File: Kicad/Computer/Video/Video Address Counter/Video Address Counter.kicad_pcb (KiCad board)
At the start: 2 copper layers, 26.7 x 90.2 mm, 22 parts, among them IC1 AP7365-33WG-7, IC10 74LVC161PW,112, IC2 74LVC573APW,118, IC3 74LVC161PW,112, IC4 74LVC161PW,112, IC5 74LVC573APW,118, IC6 74LVC161PW,112, IC7 74LVC161PW,112, IC8 74LVC573APW,118, IC9 74LVC161PW,112, J1 Conn_02x32_Counter_Clockwise

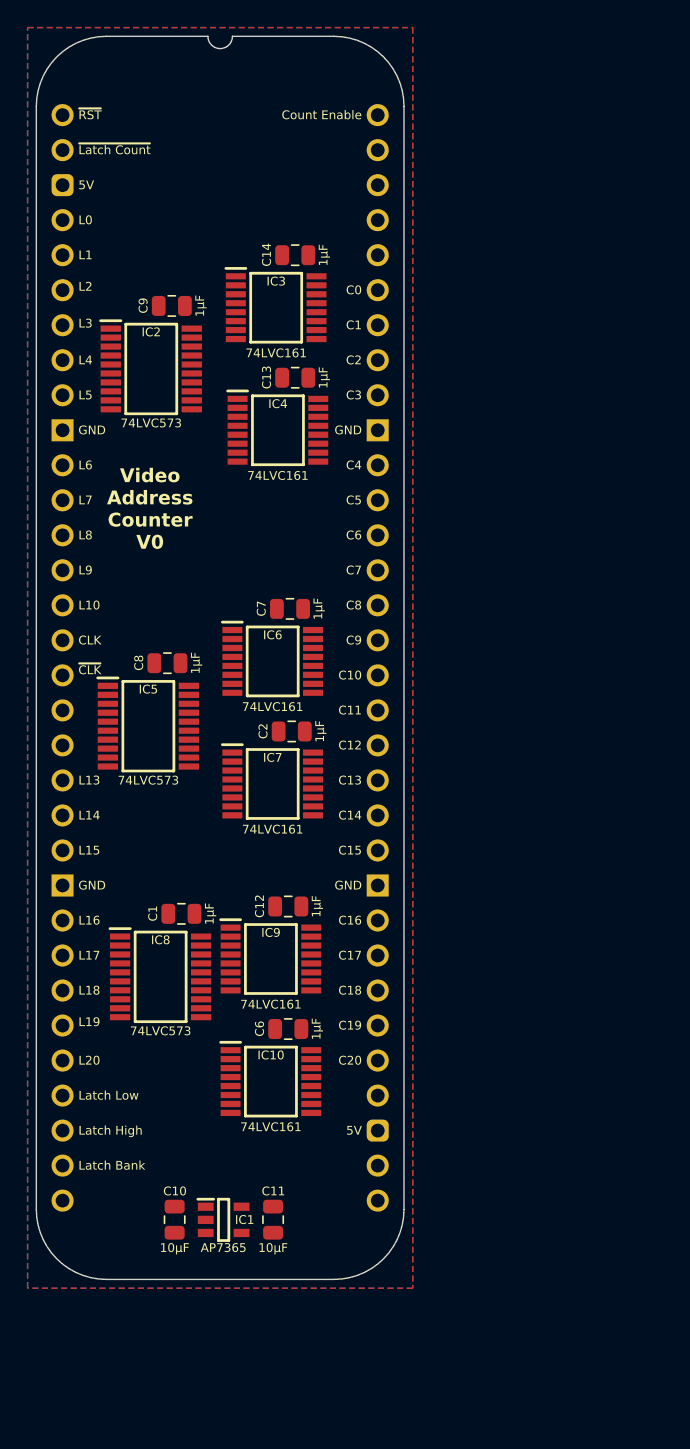
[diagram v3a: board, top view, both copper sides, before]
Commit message: Added Video Signals and Video Memory.
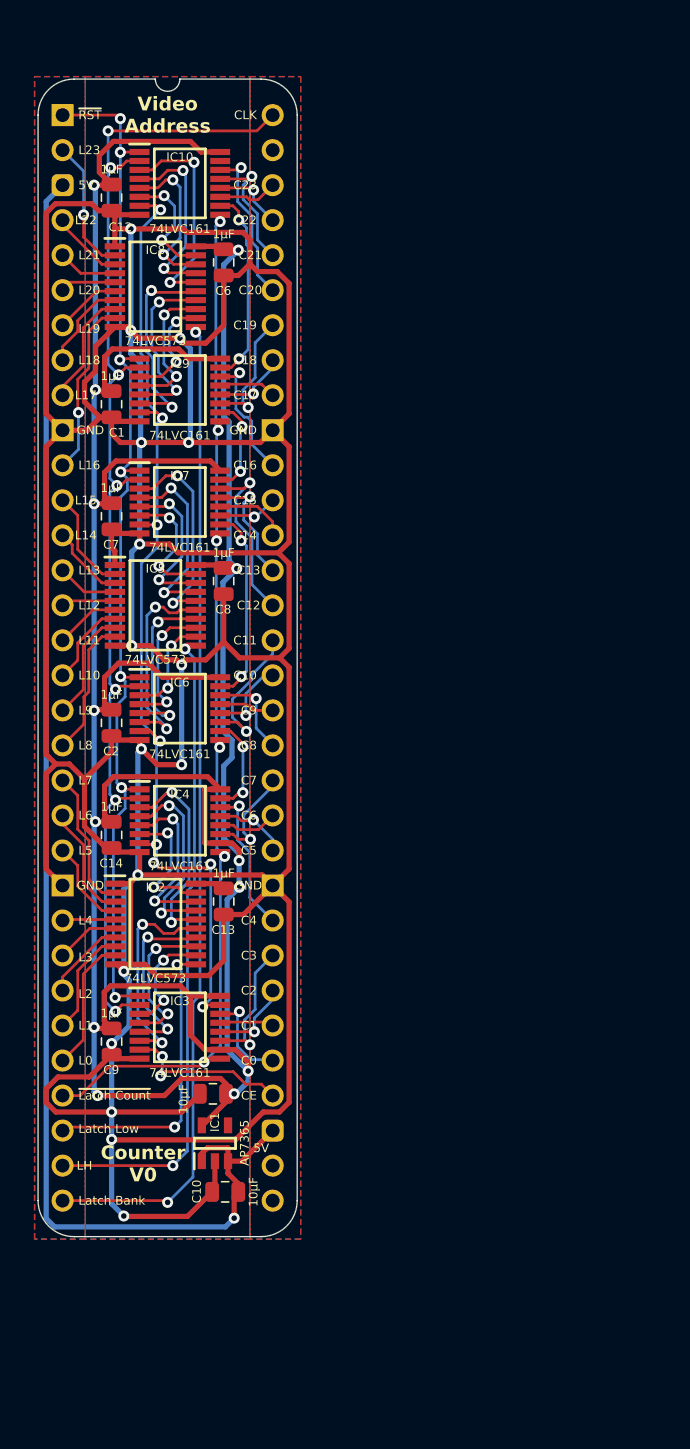
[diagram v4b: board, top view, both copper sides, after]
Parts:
- J1: footprint SamacSys_Parts:DIP-64_Board_W22.86mm -> SamacSys_Parts:DIP-64_Board_W15.24mm
- moved IC10 65.5 mm to (83.3, 53.2)
- moved C6 55.8 mm to (86.5, 58.9), turned to 180 degrees
- moved C9 53.5 mm to (78.4, 115.4), turned to 180 degrees
- moved C12 53.0 mm to (78.4, 54.2), turned to 180 degrees
- moved IC3 52.7 mm to (83.3, 114.4)
- moved IC8 50.1 mm to (81.5, 60.7)
- moved C14 44.1 mm to (78.4, 100.5), turned to 180 degrees
- moved IC9 41.8 mm to (83.3, 68.2)
- moved IC2 40.3 mm to (81.5, 106.9)
- moved C13 38.3 mm to (86.5, 105.3), turned to 180 degrees
- moved C1 37.3 mm to (78.4, 69.2), turned to 180 degrees
- moved IC4 29.2 mm to (83.3, 99.4)
- moved IC7 21.5 mm to (83.3, 76.3)
- moved C7 14.6 mm to (78.4, 77.3), turned to 180 degrees
- moved C2 13.1 mm to (78.4, 92.3), turned to 180 degrees
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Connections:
- IC10 pad 11: unconnected-(IC10-Q3-Pad11) -> /C23
- IC10 pad 12: unconnected-(IC10-Q2-Pad12) -> /C22
- IC10 pad 13: unconnected-(IC10-Q1-Pad13) -> /C21
- IC10 pad 4: /GND -> /LC21
- IC10 pad 5: /GND -> /LC22
- IC10 pad 6: /GND -> /LC23
- IC2 pad 12: /LC7 -> /LC0
- IC2 pad 13: /LC6 -> /LC1
- IC2 pad 14: /LC5 -> /LC2
- IC2 pad 15: /LC4 -> /LC3
- IC2 pad 16: /LC3 -> /LC4
- IC2 pad 17: /LC2 -> /LC5
- IC2 pad 18: /LC1 -> /LC6
- IC2 pad 19: /LC0 -> /LC7
- IC2 pad 2: /L0 -> /L7
- IC2 pad 3: /L1 -> /L6
- IC2 pad 4: /L2 -> /L5
- IC2 pad 5: /L3 -> /L4
- IC2 pad 6: /L4 -> /L3
- IC2 pad 7: /L5 -> /L2
- IC2 pad 8: /L6 -> /L1
- IC2 pad 9: /L7 -> /L0
- IC5 pad 12: /LC15 -> /LC8
- IC5 pad 13: /LC14 -> /LC9
- IC5 pad 14: /LC13 -> /LC10
- IC5 pad 15: /LC12 -> /LC11
- IC5 pad 16: /LC11 -> /LC12
- IC5 pad 17: /LC10 -> /LC13
- IC5 pad 18: /LC9 -> /LC14
- IC5 pad 19: /LC8 -> /LC15
- IC5 pad 2: /L8 -> /L15
- IC5 pad 3: /L9 -> /L14
- IC5 pad 4: /L10 -> /L13
- IC5 pad 5: /L11 -> /L12
- IC5 pad 6: /L12 -> /L11
- IC5 pad 7: /L13 -> /L10
- IC5 pad 8: /L14 -> /L9
- IC5 pad 9: /L15 -> /L8
- IC8 pad 12: unconnected-(IC8-Q7-Pad12) -> /LC16
- IC8 pad 13: unconnected-(IC8-Q6-Pad13) -> /LC17
- IC8 pad 14: unconnected-(IC8-Q5-Pad14) -> /LC18
- IC8 pad 15: /LC20 -> /LC19
- IC8 pad 16: /LC19 -> /LC20
- IC8 pad 17: /LC18 -> /LC21
- IC8 pad 18: /LC17 -> /LC22
- IC8 pad 19: /LC16 -> /LC23
- IC8 pad 2: /L16 -> /L23
- IC8 pad 3: /L17 -> /L22
- IC8 pad 4: /L18 -> /L21
- IC8 pad 5: /L19 -> /L20
- IC8 pad 6: /L20 -> /L19
- IC8 pad 7: /GND -> /L18
- IC8 pad 8: /GND -> /L17
- IC8 pad 9: /GND -> /L16
- J1 pad 11: /L6 -> /L16
- J1 pad 12: /L7 -> /L15
- J1 pad 13: /L8 -> /L14
- J1 pad 14: /L9 -> /L13
- J1 pad 15: /L10 -> /L12
- J1 pad 16: /Pixel CLK -> /L11
- J1 pad 17: /~{Pixel CLK} -> /L10
- J1 pad 18: /L11 -> /L9
- J1 pad 19: /L12 -> /L8
- J1 pad 2: /~{Latch Count} -> /L23
- J1 pad 20: /L13 -> /L7
- J1 pad 21: /L14 -> /L6
- J1 pad 22: /L15 -> /L5
- J1 pad 24: /L16 -> /L4
- J1 pad 25: /L17 -> /L3
- J1 pad 26: /L18 -> /L2
- J1 pad 27: /L19 -> /L1
- J1 pad 28: /L20 -> /L0
- J1 pad 29: /Latch Low -> /~{Latch Count}
- J1 pad 30: /Latch High -> /Latch Low
- J1 pad 31: /Latch Bank -> /Latch High
- J1 pad 32: unconnected-(J1-Pin_32-Pad32) -> /Latch Bank
- J1 pad 36: unconnected-(J1-Pin_36-Pad36) -> /Count Enable
- J1 pad 37: /C20 -> /C0
- J1 pad 38: /C19 -> /C1
- J1 pad 39: /C18 -> /C2
- J1 pad 4: /L0 -> /L22
- J1 pad 40: /C17 -> /C3
- J1 pad 41: /C16 -> /C4
- J1 pad 43: /C15 -> /C5
- J1 pad 44: /C14 -> /C6
- J1 pad 45: /C13 -> /C7
- J1 pad 46: /C12 -> /C8
- J1 pad 47: /C11 -> /C9
- J1 pad 49: /C9 -> /C11
- J1 pad 5: /L1 -> /L21
- J1 pad 50: /C8 -> /C12
- J1 pad 51: /C7 -> /C13
- J1 pad 52: /C6 -> /C14
- J1 pad 53: /C5 -> /C15
- J1 pad 54: /C4 -> /C16
- J1 pad 56: /C3 -> /C17
- J1 pad 57: /C2 -> /C18
- J1 pad 58: /C1 -> /C19
- J1 pad 59: /C0 -> /C20
- J1 pad 6: /L2 -> /L20
- J1 pad 60: unconnected-(J1-Pin_60-Pad60) -> /C21
- J1 pad 61: unconnected-(J1-Pin_61-Pad61) -> /C22
- J1 pad 62: unconnected-(J1-Pin_62-Pad62) -> /C23
- J1 pad 64: /Count Enable -> /Pixel CLK
- J1 pad 7: /L3 -> /L19
- J1 pad 8: /L4 -> /L18
- J1 pad 9: /L5 -> /L17
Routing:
- net /GND: track 0.00 -> 395.0 mm, vias 0 -> 16
- net /3.3V: track 0.00 -> 249.1 mm, vias 0 -> 13
- net /5V: track 0.00 -> 101.5 mm, vias 0 -> 1
- net /Pixel CLK: track 0.00 -> 90.0 mm, vias 0 -> 7
- net /~{Reset}: track 0.00 -> 79.0 mm, vias 0 -> 7
- net /~{Latch Count}: track 0.00 -> 77.6 mm, vias 0 -> 6
- net /TC_{0..3}: track 0.00 -> 74.0 mm, vias 0 -> 8
- net /Latch Bank: track 0.00 -> 72.3 mm, vias 0 -> 2
- net /Latch High: track 0.00 -> 46.8 mm, vias 0 -> 2
- net /Latch Low: track 0.00 -> 21.4 mm, vias 0 -> 2
- net /LC20: track 0.00 -> 15.6 mm, vias 0 -> 2
- net /LC3: track 0.00 -> 15.4 mm, vias 0 -> 2
- net /LC12: track 0.00 -> 15.2 mm, vias 0 -> 2
- net /LC4: track 0.00 -> 15.2 mm, vias 0 -> 2
- net /LC19: track 0.00 -> 15.1 mm, vias 0 -> 2
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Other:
- board size 26.7 x 90.2 mm -> 18.8 x 84 mm
- board text added: "C21"
- board text added: "C22"
- board text added: "C23"
- board text added: "CE"
- board text added: "Counter V0"
- board text added: "L11"
- board text added: "L12"
- board text added: "L21"
- board text added: "L22"
- board text added: "L23"
- board text added: "LH"
- board text added: "Video Address"
- board text removed: "Count Enable"
- board text removed: "Latch High"
- board text removed: "Video Address Counter V0"
- board text removed: "~{CLK}"

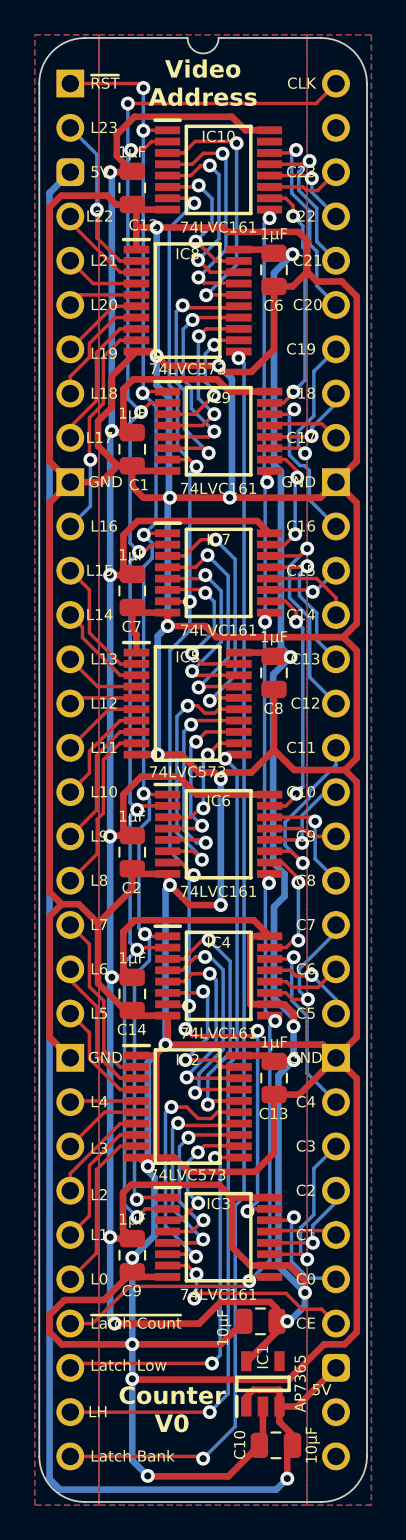
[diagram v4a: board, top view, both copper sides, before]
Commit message: Added Video Memory 2MB and D-type Flip Flop 16bit.
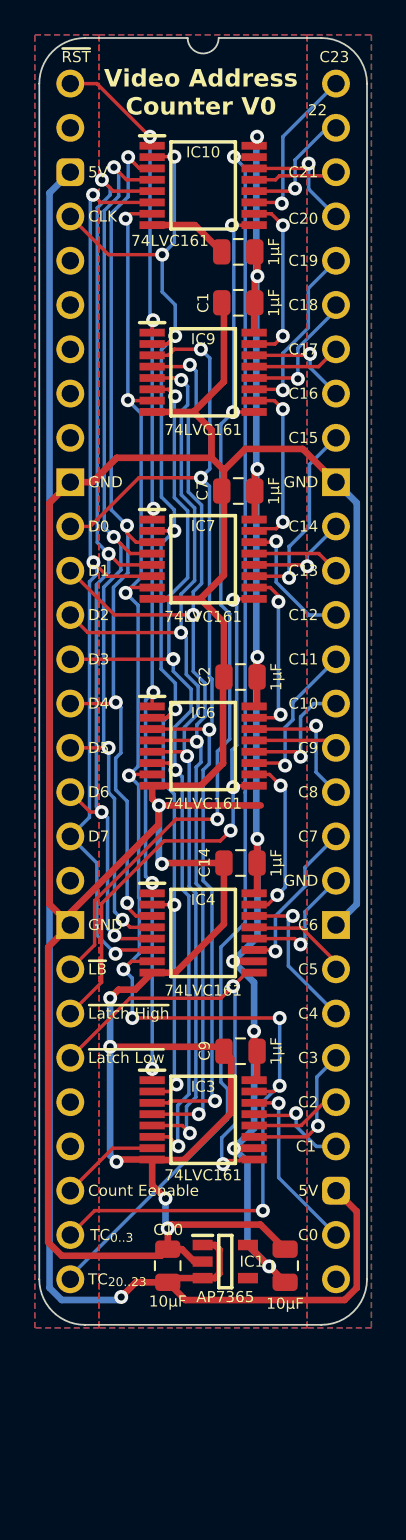
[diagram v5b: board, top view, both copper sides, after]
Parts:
- removed C13, C6, C8: 1μF, SamacSys_Parts:C_0805
- removed IC2, IC5, IC8: 74LVC573APW,118, SamacSys_Parts:SOP65P640X110-20N
- J1: footprint SamacSys_Parts:DIP-64_Board_W15.24mm -> SamacSys_Parts:DIP-56_Board_W15.24mm
- moved C9 13.2 mm to (84.6, 103.8), turned to 90 degrees
- moved C10 12.0 mm to (80.4, 116.1), turned to 0 degrees
- moved C2 11.8 mm to (84.6, 82.3), turned to 90 degrees
- moved C1 10.4 mm to (84.5, 60.8), turned to 90 degrees
- moved C14 9.74 mm to (84.6, 93.0), turned to 90 degrees
- moved C7 8.36 mm to (84.5, 71.6), turned to 90 degrees
- moved IC1 7.34 mm to (83.7, 115.8), turned to 0 degrees
- moved C12 7.13 mm to (84.5, 57.9), turned to 90 degrees
- moved IC3 6.79 mm to (82.4, 107.7)
- moved IC6 5.13 mm to (82.4, 86.3)
- moved IC9 3.49 mm to (82.4, 64.8)
- moved C11 3.47 mm to (87.1, 116.1), turned to 0 degrees
- moved IC4 2.62 mm to (82.4, 97.0)
- moved IC10 1.25 mm to (82.4, 54.1)
- moved IC7 1.18 mm to (82.4, 75.5)
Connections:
- IC10 pad 15: unconnected-(IC10-TC-Pad15) -> /TC_{20..23}
- IC10 pad 2: /Pixel CLK -> /CLK
- IC10 pad 3: /LC20 -> /D4
- IC10 pad 4: /LC21 -> /D5
- IC10 pad 5: /LC22 -> /D6
- IC10 pad 6: /LC23 -> /D7
- IC10 pad 9: /~{Latch Count} -> /~{Latch Bank}
- IC3 pad 2: /Pixel CLK -> /CLK
- IC3 pad 3: /LC0 -> /D0
- IC3 pad 4: /LC1 -> /D1
- IC3 pad 5: /LC2 -> /D2
- IC3 pad 6: /LC3 -> /D3
- IC3 pad 9: /~{Latch Count} -> /~{Latch Low}
- IC4 pad 2: /Pixel CLK -> /CLK
- IC4 pad 3: /LC4 -> /D4
- IC4 pad 4: /LC5 -> /D5
- IC4 pad 5: /LC6 -> /D6
- IC4 pad 6: /LC7 -> /D7
- IC4 pad 9: /~{Latch Count} -> /~{Latch Low}
- IC6 pad 2: /Pixel CLK -> /CLK
- IC6 pad 3: /LC8 -> /D0
- IC6 pad 4: /LC9 -> /D1
- IC6 pad 5: /LC10 -> /D2
- IC6 pad 6: /LC11 -> /D3
- IC6 pad 9: /~{Latch Count} -> /~{Latch High}
- IC7 pad 2: /Pixel CLK -> /CLK
- IC7 pad 3: /LC12 -> /D4
- IC7 pad 4: /LC13 -> /D5
- IC7 pad 5: /LC14 -> /D6
- IC7 pad 6: /LC15 -> /D7
- IC7 pad 9: /~{Latch Count} -> /~{Latch High}
- IC9 pad 2: /Pixel CLK -> /CLK
- IC9 pad 3: /LC16 -> /D0
- IC9 pad 4: /LC17 -> /D1
- IC9 pad 5: /LC18 -> /D2
- IC9 pad 6: /LC19 -> /D3
- IC9 pad 9: /~{Latch Count} -> /~{Latch Bank}
- J1 pad 11: /L16 -> /D0
- J1 pad 12: /L15 -> /D1
- J1 pad 13: /L14 -> /D2
- J1 pad 14: /L13 -> /D3
- J1 pad 15: /L12 -> /D4
- J1 pad 16: /L11 -> /D5
- J1 pad 17: /L10 -> /D6
- J1 pad 18: /L9 -> /D7
- J1 pad 19: /L8 -> unconnected-(J1-Pin_19-Pad19)
- J1 pad 2: /L23 -> unconnected-(J1-Pin_2-Pad2)
- J1 pad 20: /L7 -> /GND
- J1 pad 21: /L6 -> /~{Latch Bank}
- J1 pad 22: /L5 -> /~{Latch High}
- J1 pad 23: /GND -> /~{Latch Low}
- J1 pad 24: /L4 -> unconnected-(J1-Pin_24-Pad24)
- J1 pad 25: /L3 -> unconnected-(J1-Pin_25-Pad25)
- J1 pad 26: /L2 -> /Count Enable
- J1 pad 27: /L1 -> /TC_{0..3}
- J1 pad 28: /L0 -> /TC_{20..23}
- J1 pad 29: /~{Latch Count} -> unconnected-(J1-Pin_29-Pad29)
- J1 pad 30: /Latch Low -> /C0
- J1 pad 31: /Latch High -> /5V
- J1 pad 32: /Latch Bank -> /C1
- J1 pad 33: unconnected-(J1-Pin_33-Pad33) -> /C2
- J1 pad 34: unconnected-(J1-Pin_34-Pad34) -> /C3
- J1 pad 35: /5V -> /C4
- J1 pad 36: /Count Enable -> /C5
- J1 pad 37: /C0 -> /GND
- J1 pad 38: /C1 -> /C6
- J1 pad 39: /C2 -> /C7
- J1 pad 4: /L22 -> /CLK
- J1 pad 40: /C3 -> /C8
- J1 pad 41: /C4 -> /C9
- J1 pad 42: /GND -> /C10
- J1 pad 43: /C5 -> /C11
- J1 pad 44: /C6 -> /C12
- J1 pad 45: /C7 -> /C13
- J1 pad 46: /C8 -> /C14
- J1 pad 47: /C9 -> /GND
- J1 pad 48: /C10 -> /C15
- J1 pad 49: /C11 -> /C16
- J1 pad 5: /L21 -> unconnected-(J1-Pin_5-Pad5)
- J1 pad 50: /C12 -> /C17
- J1 pad 51: /C13 -> /C18
- J1 pad 52: /C14 -> /C19
- J1 pad 53: /C15 -> /C20
- J1 pad 54: /C16 -> /C21
- J1 pad 55: /GND -> /C22
- J1 pad 56: /C17 -> /C23
- J1 pad 6: /L20 -> unconnected-(J1-Pin_6-Pad6)
- J1 pad 7: /L19 -> unconnected-(J1-Pin_7-Pad7)
- J1 pad 8: /L18 -> unconnected-(J1-Pin_8-Pad8)
- J1 pad 9: /L17 -> unconnected-(J1-Pin_9-Pad9)
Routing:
- net /GND: track 395.0 -> 215.2 mm, vias 16 -> 7
- net /3.3V: track 249.1 -> 89.6 mm, vias 13 -> 9
- net /Pixel CLK: track 90.0 -> 0.00 mm, vias 7 -> 0
- net /~{Latch Count}: track 77.6 -> 0.00 mm, vias 6 -> 0
- net /Latch Bank: track 72.3 -> 0.00 mm, vias 2 -> 0
- net /CLK: track 0.00 -> 70.3 mm, vias 0 -> 7
- net /TC_{20..23}: track 0.00 -> 70.1 mm, vias 0 -> 1
- net /D0: track 0.00 -> 62.8 mm, vias 0 -> 4
- net /D1: track 0.00 -> 60.3 mm, vias 0 -> 4
- net /D2: track 0.00 -> 58.4 mm, vias 0 -> 4
- net /D3: track 0.00 -> 56.0 mm, vias 0 -> 4
- net /D6: track 0.00 -> 55.2 mm, vias 0 -> 4
- net /D7: track 0.00 -> 54.9 mm, vias 0 -> 3
- net /D5: track 0.00 -> 54.0 mm, vias 0 -> 4
- net /D4: track 0.00 -> 52.8 mm, vias 0 -> 4
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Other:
- board size 18.8 x 84 mm -> 18.8 x 73.8 mm
- board text added: "22"
- board text added: "Count Eenable"
- board text added: "D0"
- board text added: "D1"
- board text added: "D2"
- board text added: "D3"
- board text added: "D4"
- board text added: "D5"
- board text added: "D6"
- board text added: "D7"
- board text added: "TC_{0..3}"
- board text added: "TC_{20..23}"
- board text added: "Video Address Counter V0"
- board text added: "~{LB}"
- board text added: "~{Latch High}"
- board text added: "~{Latch Low}"
- board text removed: "C22"
- board text removed: "CE"
- board text removed: "Counter V0"
- board text removed: "L0"
- board text removed: "L1"
- board text removed: "L10"
- board text removed: "L11"
- board text removed: "L12"
- board text removed: "L13"
- board text removed: "L14"
- board text removed: "L15"
- board text removed: "L16"
- board text removed: "L17"
- board text removed: "L18"
- board text removed: "L19"
- board text removed: "L2"
- board text removed: "L20"
- board text removed: "L21"
- board text removed: "L22"
- board text removed: "L23"
- board text removed: "L3"
- board text removed: "L4"
- board text removed: "L5"
- board text removed: "L6"
- board text removed: "L7"
- board text removed: "L8"
- board text removed: "L9"
- board text removed: "LH"
- board text removed: "Latch Bank"
- board text removed: "Latch Low"
- board text removed: "Video Address"
- board text removed: "~{Latch Count}"

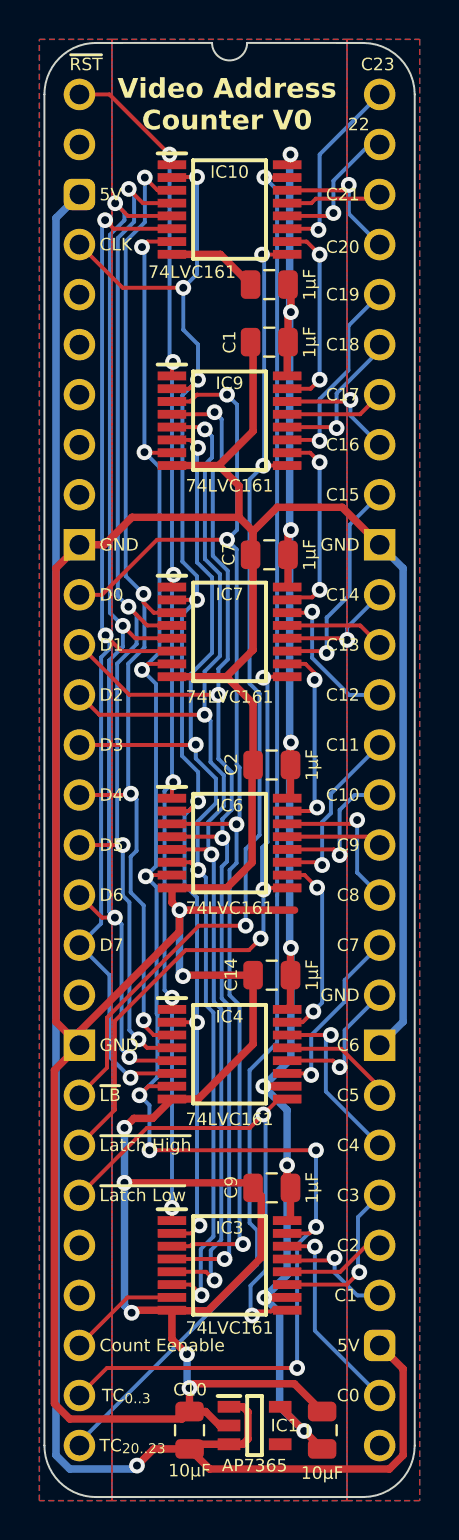
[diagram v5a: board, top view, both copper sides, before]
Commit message: Auto-routed Video memory and signal boards.  Flipped the data pins on Video Video Address Counter.
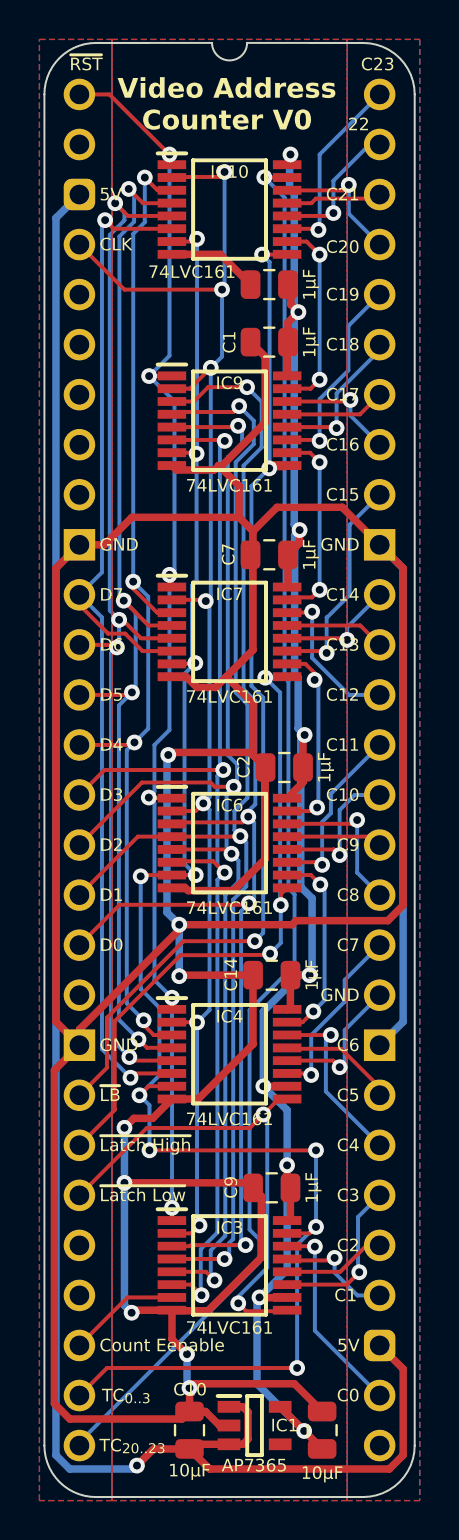
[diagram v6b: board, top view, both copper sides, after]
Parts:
- moved C2 0.65 mm to (85.2, 82.4)
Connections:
- J1 pad 11: /D0 -> /D7
- J1 pad 12: /D1 -> /D6
- J1 pad 13: /D2 -> /D5
- J1 pad 14: /D3 -> /D4
- J1 pad 15: /D4 -> /D3
- J1 pad 16: /D5 -> /D2
- J1 pad 17: /D6 -> /D1
- J1 pad 18: /D7 -> /D0
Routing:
- net /GND: track 215.2 -> 253.5 mm, vias 7 -> 8
- net /D2: track 58.4 -> 63.2 mm
- net /CLK: track 70.3 -> 74.2 mm
- net /D0: track 62.8 -> 66.4 mm
- net /D3: track 56.0 -> 59.4 mm
- net /3.3V: track 89.6 -> 92.2 mm
- net /~{Reset}: track 63.9 -> 66.1 mm
- net /D7: track 54.9 -> 56.6 mm, vias 3 -> 2
- net /~{Latch High}: track 32.2 -> 33.1 mm
- net /TC_{20..23}: track 70.1 -> 70.9 mm
- net /~{Latch Bank}: track 50.9 -> 51.7 mm
- net /D5: track 54.0 -> 54.7 mm
- net /D4: track 52.8 -> 53.3 mm
- net /TC_{0..3}: track 89.0 -> 89.5 mm, vias 9 -> 10
- net /D1: track 60.3 -> 60.7 mm, vias 4 -> 3
